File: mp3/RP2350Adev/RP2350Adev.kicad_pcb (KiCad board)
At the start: 2 copper layers, 30.9 x 51.8 mm, 44 parts, among them J1 USB4105-GF-A, J2 LEFT, J4 RIGHT, U1 W25Q32JV, U2 RP2350A, U3 MCP1702T-3302E_CB, X1 IQXO-791

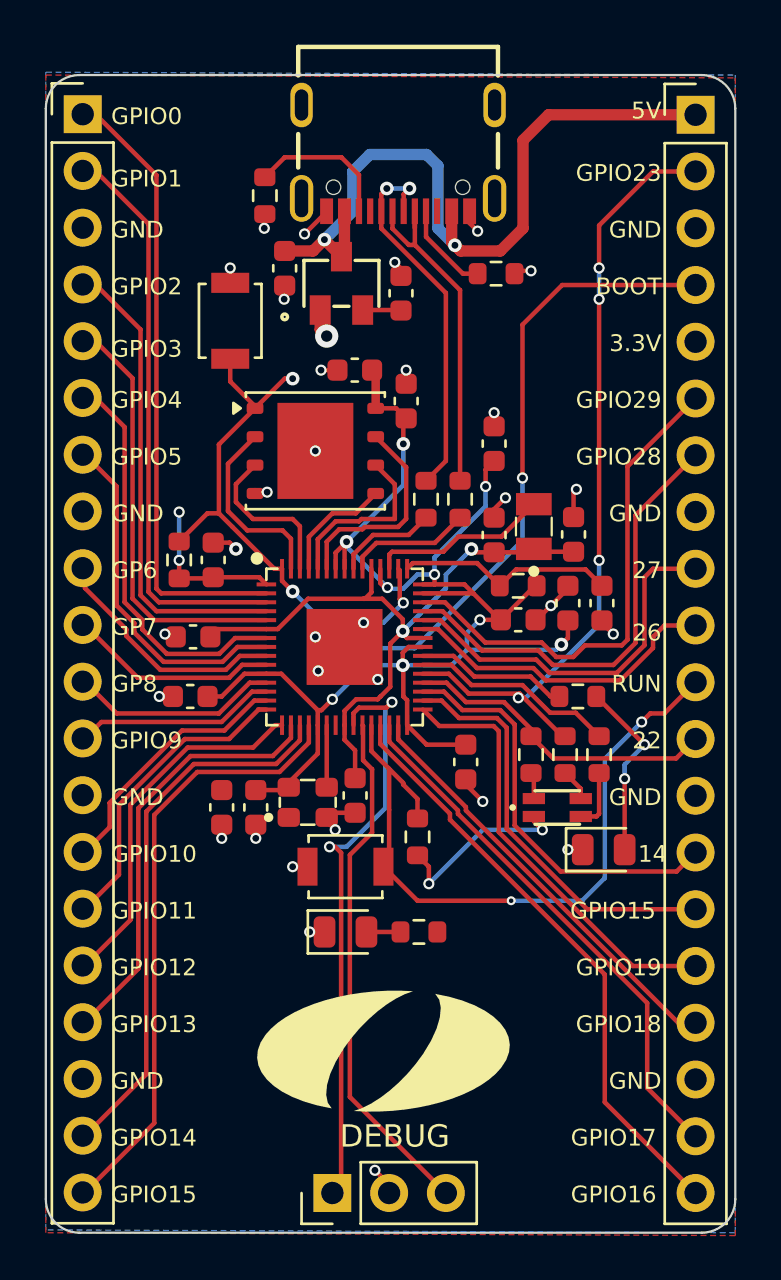
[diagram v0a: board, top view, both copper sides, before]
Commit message: Update silkscreen thickness/width for DRC
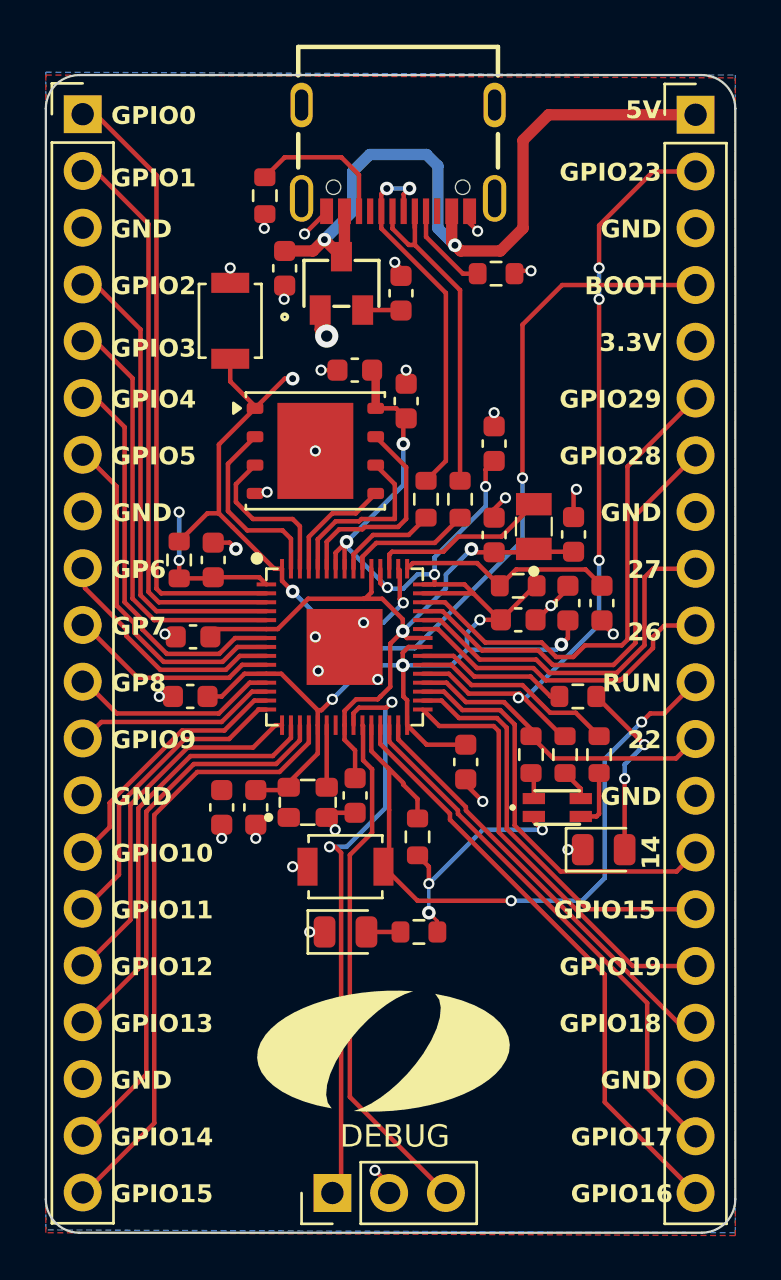
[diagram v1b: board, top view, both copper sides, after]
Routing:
- net +3V3: track 86.2 -> 88.5 mm, vias 13 -> 14
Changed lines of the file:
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@@
 		(effects
 			(font
-				(size 0.75 0.75)
-				(thickness 0.12)
+				(size 0.8 0.8)
+				(thickness 0.15)
+				(bold yes)
 			)
 			(justify right bottom)
@@
 		(effects
 			(font
-				(size 0.75 0.75)
-				(thickness 0.12)
+				(size 0.8 0.8)
+				(thickness 0.15)
+				(bold yes)
 			)
 			(justify left bottom)
@@
 		(effects
 			(font
-				(size 0.75 0.75)
-				(thickness 0.12)
+				(size 0.8 0.8)
+				(thickness 0.15)
+				(bold yes)
 			)
 			(justify right bottom)
@@
 		(effects
 			(font
-				(size 0.75 0.75)
-				(thickness 0.12)
+				(size 0.8 0.8)
+				(thickness 0.15)
+				(bold yes)
 			)
 			(justify left bottom)
@@
 		(effects
 			(font
-				(size 0.75 0.75)
-				(thickness 0.12)
+				(size 0.8 0.8)
+				(thickness 0.15)
+				(bold yes)
 			)
 			(justify right bottom)
@@
 		(effects
 			(font
-				(size 0.75 0.75)
-				(thickness 0.12)
+				(size 0.8 0.8)
+				(thickness 0.15)
+				(bold yes)
 			)
 			(justify right bottom)
@@
 		(effects
 			(font
-				(size 0.75 0.75)
-				(thickness 0.12)
+				(size 0.8 0.8)
+				(thickness 0.15)
+				(bold yes)
 			)
 			(justify left bottom)
@@
 		(effects
 			(font
-				(size 0.75 0.75)
-				(thickness 0.12)
+				(size 0.8 0.8)
+				(thickness 0.15)
+				(bold yes)
 			)
 			(justify right bottom)
@@
 		(effects
 			(font
-				(size 0.75 0.75)
-				(thickness 0.12)
+				(size 0.8 0.8)
+				(thickness 0.15)
+				(bold yes)
 			)
 			(justify left bottom)
@@
 		(effects
 			(font
-				(size 0.75 0.75)
-				(thickness 0.12)
+				(size 0.8 0.8)
+				(thickness 0.15)
+				(bold yes)
 			)
 			(justify right bottom)
@@
 		(effects
 			(font
-				(size 0.75 0.75)
-				(thickness 0.12)
+				(size 0.8 0.8)
+				(thickness 0.15)
+				(bold yes)
 			)
 			(justify left bottom)
@@
 		(effects
 			(font
-				(size 0.75 0.75)
-				(thickness 0.12)
+				(size 0.8 0.8)
+				(thickness 0.15)
+				(bold yes)
 			)
 			(justify left bottom)
@@
 		(effects
 			(font
-				(size 0.75 0.75)
-				(thickness 0.12)
+				(size 0.8 0.8)
+				(thickness 0.15)
+				(bold yes)
 			)
 			(justify right bottom)
@@
 		(effects
 			(font
-				(size 0.75 0.75)
-				(thickness 0.12)
+				(size 0.8 0.8)
+				(thickness 0.15)
+				(bold yes)
 			)
 			(justify right bottom)
@@
 		(effects
 			(font
-				(size 0.75 0.75)
-				(thickness 0.12)
+				(size 0.8 0.8)
+				(thickness 0.15)
+				(bold yes)
 			)
 			(justify left bottom)
@@
 		(effects
 			(font
-				(size 0.75 0.75)
-				(thickness 0.12)
+				(size 0.8 0.8)
+				(thickness 0.15)
+				(bold yes)
 			)
 			(justify left bottom)
@@
 		(effects
 			(font
-				(size 0.75 0.75)
-				(thickness 0.12)
+				(size 0.8 0.8)
+				(thickness 0.15)
+				(bold yes)
 			)
 			(justify left bottom)
@@
 		(effects
 			(font
-				(size 0.75 0.75)
-				(thickness 0.12)
+				(size 0.8 0.8)
+				(thickness 0.15)
+				(bold yes)
 			)
 			(justify left bottom)
@@
 		(effects
 			(font
-				(size 0.75 0.75)
-				(thickness 0.12)
+				(size 0.8 0.8)
+				(thickness 0.15)
+				(bold yes)
 			)
 			(justify left bottom)
@@
 		(effects
 			(font
-				(size 0.75 0.75)
-				(thickness 0.12)
+				(size 0.8 0.8)
+				(thickness 0.15)
+				(bold yes)
 			)
 			(justify left bottom)
@@
 		(effects
 			(font
-				(size 0.75 0.75)
-				(thickness 0.12)
+				(size 0.8 0.8)
+				(thickness 0.15)
+				(bold yes)
 			)
 			(justify right bottom)
@@
 		(effects
 			(font
-				(size 0.75 0.75)
-				(thickness 0.12)
+				(size 0.8 0.8)
+				(thickness 0.15)
+				(bold yes)
 			)
 			(justify right bottom)
@@
 		(effects
 			(font
-				(size 0.75 0.75)
-				(thickness 0.12)
+				(size 0.8 0.8)
+				(thickness 0.15)
+				(bold yes)
 			)
 			(justify right bottom)
@@
 		(effects
 			(font
-				(size 0.75 0.75)
-				(thickness 0.12)
+				(size 0.8 0.8)
+				(thickness 0.15)
+				(bold yes)
 			)
 			(justify left bottom)
@@
 		(effects
 			(font
-				(size 0.75 0.75)
-				(thickness 0.12)
+				(size 0.8 0.8)
+				(thickness 0.15)
+				(bold yes)
 			)
 			(justify left bottom)
@@
 		(effects
 			(font
-				(size 0.75 0.75)
-				(thickness 0.12)
+				(size 0.8 0.8)
+				(thickness 0.15)
+				(bold yes)
 			)
 			(justify left bottom)
@@
 		(effects
 			(font
-				(size 0.75 0.75)
-				(thickness 0.12)
+				(size 0.8 0.8)
+				(thickness 0.15)
+				(bold yes)
 			)
 			(justify right bottom)
@@
 	)
 	(gr_text "14"
-		(at 55.118 58.166 0)
+		(at 54.864 56.896 90)
 		(layer "F.SilkS")
 		(effects
 			(font
-				(size 0.75 0.75)
-				(thickness 0.12)
+				(size 0.8 0.8)
+				(thickness 0.15)
+				(bold yes)
 			)
 			(justify right bottom)
@@
 		(effects
 			(font
-				(size 0.75 0.75)
-				(thickness 0.12)
+				(size 0.8 0.8)
+				(thickness 0.15)
+				(bold yes)
 			)
 			(justify right bottom)
@@
 		(effects
 			(font
-				(size 0.75 0.75)
-				(thickness 0.12)
+				(size 0.8 0.8)
+				(thickness 0.15)
+				(bold yes)
 			)
 			(justify left bottom)
@@
 		(effects
 			(font
-				(size 0.75 0.75)
-				(thickness 0.12)
+				(size 0.8 0.8)
+				(thickness 0.15)
+				(bold yes)
 			)
 			(justify left bottom)
@@
 		(effects
 			(font
-				(size 0.75 0.75)
-				(thickness 0.12)
+				(size 0.8 0.8)
+				(thickness 0.15)
+				(bold yes)
 			)
 			(justify right bottom)
@@
 		(effects
 			(font
-				(size 0.75 0.75)
-				(thickness 0.12)
+				(size 0.8 0.8)
+				(thickness 0.15)
+				(bold yes)
 			)
 			(justify right bottom)
@@
 		(effects
 			(font
-				(size 0.75 0.75)
-				(thickness 0.12)
+				(size 0.8 0.8)
+				(thickness 0.15)
+				(bold yes)
 			)
 			(justify left bottom)
@@
 		(effects
 			(font
-				(size 0.75 0.75)
-				(thickness 0.12)
+				(size 0.8 0.8)
+				(thickness 0.15)
+				(bold yes)
 			)
 			(justify left bottom)
@@
 		(effects
 			(font
-				(size 0.75 0.75)
-				(thickness 0.12)
+				(size 0.8 0.8)
+				(thickness 0.15)
+				(bold yes)
 			)
 			(justify left bottom)
@@
 		(effects
 			(font
-				(size 0.75 0.75)
-				(thickness 0.12)
+				(size 0.8 0.8)
+				(thickness 0.15)
+				(bold yes)
 			)
 			(justify left bottom)
@@
 		(effects
 			(font
-				(size 0.75 0.75)
-				(thickness 0.12)
+				(size 0.8 0.8)
+				(thickness 0.15)
+				(bold yes)
 			)
 			(justify right bottom)
@@
 		(effects
 			(font
-				(size 0.75 0.75)
-				(thickness 0.12)
+				(size 0.8 0.8)
+				(thickness 0.15)
+				(bold yes)
 			)
 			(justify right bottom)
@@
 		(effects
 			(font
-				(size 0.75 0.75)
-				(thickness 0.12)
+				(size 0.8 0.8)
+				(thickness 0.15)
+				(bold yes)
 			)
 			(justify left bottom)
@@
 	)
 	(segment
+		(start 44.83 61.214)
+		(end 44.83 60.7304)
+		(width 0.1524)
+		(layer "F.Cu")
+		(net 1)
+	)
+	(segment
 		(start 42.07 37.778)
 		(end 42.07 36.228)
@@
 	)
 	(segment
+		(start 44.83 60.7304)
+		(end 44.45 60.3504)
+		(width 0.1524)
+		(layer "F.Cu")
+		(net 1)
+	)
+	(segment
 		(start 50.380822 48.348822)
 		(end 50.673 48.056644)
@@
 	)
 	(via
+		(at 44.45 60.3504)
+		(size 0.6096)
+		(drill 0.3048)
+		(layers "F.Cu" "B.Cu")
+		(net 1)
+	)
+	(via
 		(at 44.704 45.212)
 		(size 0.5)
@@
 	)
 	(segment
+		(start 44.45 60.3504)
+		(end 44.45 59.055)
+		(width 0.1524)
+		(layer "B.Cu")
+		(net 1)
+	)
+	(segment
 		(start 42.596197 45.797902)
 		(end 42.596197 45.668803)
@@
 	(via
 		(at 48.133 59.817)
-		(size 0.4)
-		(drill 0.2)
+		(size 0.5)
+		(drill 0.3)
 		(layers "F.Cu" "B.Cu")
 		(net 44)

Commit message: Update silkscreen overlap
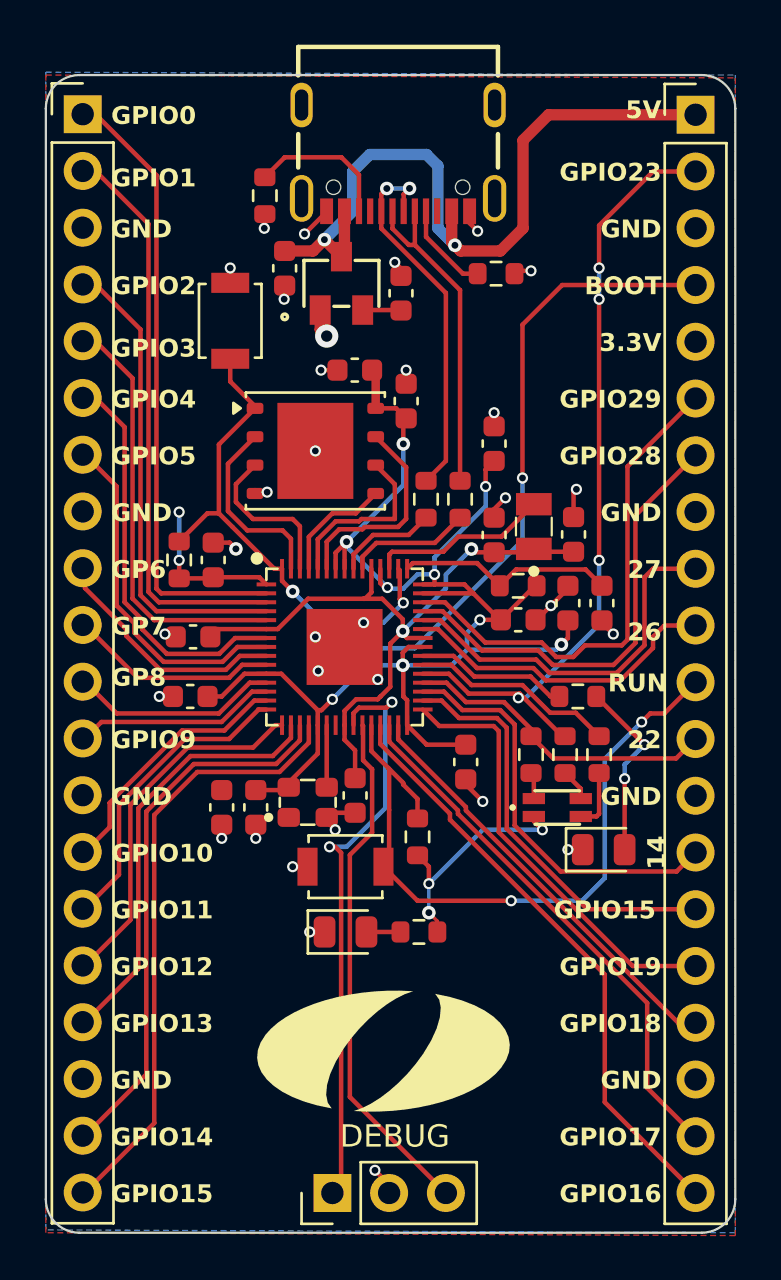
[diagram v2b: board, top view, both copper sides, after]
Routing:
- net /BOOT: track 49.3 -> 47.1 mm, vias 3 -> 2
- net Net-(J1-D--PadA7): track 15.7 -> 15.0 mm
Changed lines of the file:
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@@
 	)
 	(gr_text "RUN"
-		(at 54.864 50.546 0)
+		(at 55.118 50.546 0)
 		(layer "F.SilkS")
 		(effects
@@
 	)
 	(gr_text "GPIO17"
-		(at 50.8 70.866 0)
+		(at 50.292 70.866 0)
 		(layer "F.SilkS")
 		(effects
@@
 	)
 	(gr_text "GP8"
-		(at 30.226 50.546 0)
+		(at 30.226 50.292 0)
 		(layer "F.SilkS")
 		(effects
@@
 	)
 	(gr_text "14"
-		(at 54.864 56.896 90)
+		(at 55.118 56.896 90)
 		(layer "F.SilkS")
 		(effects
@@
 	)
 	(gr_text "GPIO16"
-		(at 50.8 73.406 0)
+		(at 50.292 73.406 0)
 		(layer "F.SilkS")
 		(effects
@@
 	)
 	(segment
-		(start 44.352 52.832)
-		(end 43.478 51.958)
-		(width 0.2032)
-		(layer "F.Cu")
-		(net 1)
-	)
-	(segment
 		(start 39.478 51.289)
 		(end 39.478 51.958)
@@
 	)
 	(segment
-		(start 45.974 52.832)
-		(end 44.352 52.832)
-		(width 0.2032)
-		(layer "F.Cu")
-		(net 1)
-	)
-	(segment
 		(start 38.051 54.864)
 		(end 38.178 54.737)
@@
 	)
 	(segment
+		(start 44.352 52.832)
+		(end 43.478 51.958)
+		(width 0.2032)
+		(layer "F.Cu")
+		(net 1)
+	)
+	(segment
 		(start 44.83 60.7304)
 		(end 44.45 60.3504)
@@
 	)
 	(segment
+		(start 45.974 52.832)
+		(end 44.352 52.832)
+		(width 0.2032)
+		(layer "F.Cu")
+		(net 1)
+	)
+	(segment
 		(start 49.149 56.261)
 		(end 49.53 56.642)
@@
 	)
 	(segment
-		(start 43.823 29.702)
-		(end 43.823 28.956)
-		(width 0.2032)
-		(layer "F.Cu")
-		(net 14)
-	)
-	(segment
 		(start 45.847 41.021)
 		(end 45.847 32.488)
@@
 	)
 	(segment
-		(start 36.67 37.778)
-		(end 37.999 36.449)
-		(width 0.2032)
-		(layer "F.Cu")
-		(net 45)
-	)
-	(segment
 		(start 50.419 32.258)
 		(end 48.641 34.036)
@@
 	)
 	(segment
-		(start 37.999 36.449)
-		(end 38.354 36.449)
-		(width 0.2032)
-		(layer "F.Cu")
-		(net 45)
-	)
-	(segment
 		(start 36.67 37.686)
 		(end 35.56 36.576)
@@
 		(layers "F.Cu" "B.Cu")
 		(net 45)
-	)
-	(via
-		(at 38.354 36.449)
-		(size 0.6096)
-		(drill 0.3048)
-		(layers "F.Cu" "B.Cu")
-		(net 45)

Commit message: Update minimum via size to 24 mils
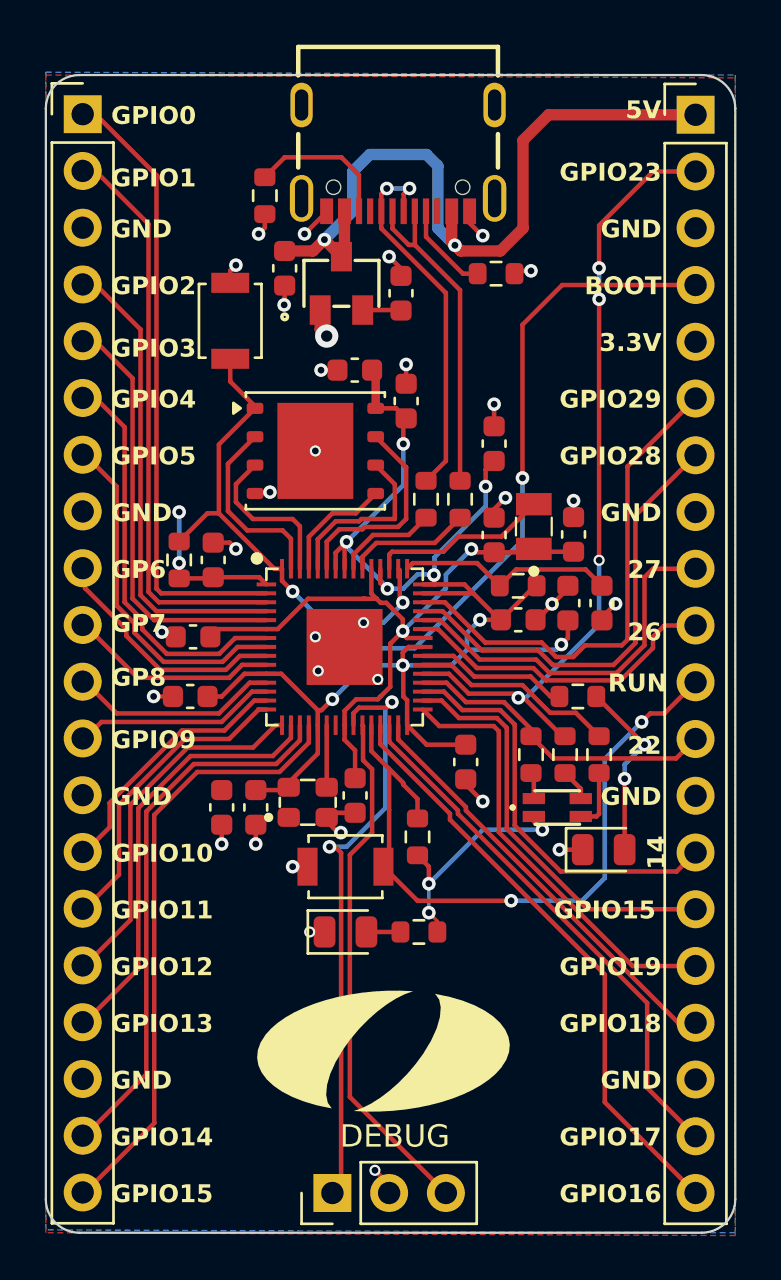
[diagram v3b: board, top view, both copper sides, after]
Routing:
- net GND: track 37.4 -> 40.9 mm

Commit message: Update missed undersized vias to 24 mils
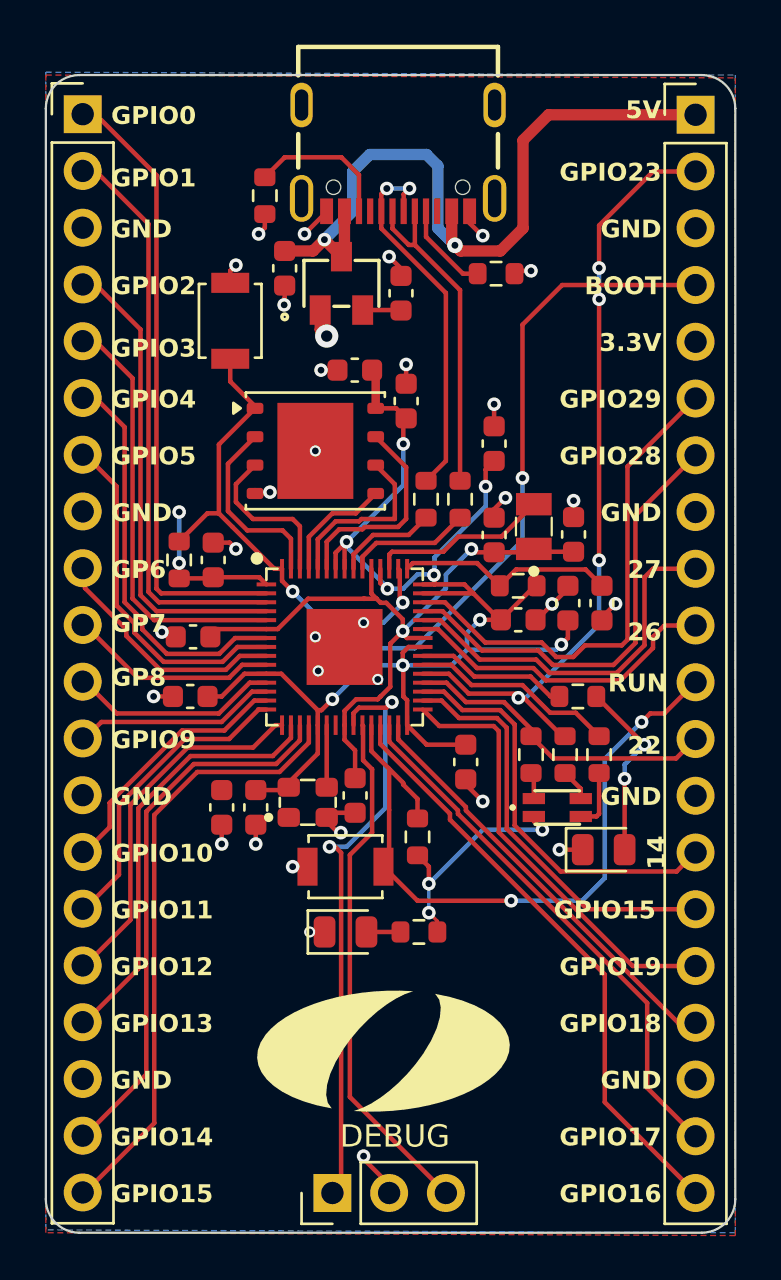
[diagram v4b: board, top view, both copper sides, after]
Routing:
- net GND: track 40.9 -> 41.7 mm
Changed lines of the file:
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@@
-	)
-	(segment
-		(start 42.672 72.517)
-		(end 42.037 71.882)
-		(width 0.2032)
-		(layer "F.Cu")
-		(net 2)
 	)
 	(segment
@@
 	)
 	(segment
+		(start 42.672 72.517)
+		(end 42.672 72.898)
+		(width 0.2032)
+		(layer "F.Cu")
+		(net 2)
+	)
+	(segment
 		(start 43.146799 45.026799)
 		(end 43.078 44.958)
@@
 	)
 	(segment
+		(start 41.529 71.247)
+		(end 41.529 71.374)
+		(width 0.2032)
+		(layer "F.Cu")
+		(net 2)
+	)
+	(segment
 		(start 32.500683 47.791399)
 		(end 32.551399 47.791399)
@@
 	)
 	(segment
-		(start 42.672 72.898)
-		(end 42.672 72.517)
-		(width 0.2032)
-		(layer "F.Cu")
-		(net 2)
-	)
-	(segment
 		(start 37.338 41.529)
 		(end 37.211 41.529)
@@
 	)
 	(segment
+		(start 41.529 71.374)
+		(end 42.672 72.517)
+		(width 0.2032)
+		(layer "F.Cu")
+		(net 2)
+	)
+	(segment
 		(start 37.152 41.588)
 		(end 36.67 41.588)
@@
 	)
 	(via
-		(at 42.037 71.882)
-		(size 0.5)
+		(at 41.529 71.247)
+		(size 0.6096)
 		(drill 0.3)
 		(layers "F.Cu" "B.Cu")
@@
 	(via
 		(at 45.617 30.48)
-		(size 0.6096)
+		(size 0.7)
 		(drill 0.3048)
 		(layers "F.Cu" "B.Cu")
@@
 	(via
 		(at 52.07 44.577)
-		(size 0.5)
-		(drill 0.3)
-		(layers "F.Cu" "B.Cu")
+		(size 0.6096)
+		(drill 0.3)
+		(layers "F.Cu" "B.Cu")

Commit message: Update ground pad vias to 24 mils
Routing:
- net GND: track 41.7 -> 42.2 mm, vias 33 -> 32
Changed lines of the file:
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@@
+	)
+	(segment
+		(start 50.927 41.656)
+		(end 50.927 42.646)
+		(width 0.2032)
+		(layer "F.Cu")
+		(net 2)
 	)
 	(segment
@@
 		(start 40.569 48.458)
 		(end 39.497 49.53)
+		(width 0.2032)
+		(layer "F.Cu")
+		(net 2)
+	)
+	(segment
+		(start 39.781 61.214)
+		(end 38.862 61.214)
 		(width 0.2032)
 		(layer "F.Cu")
@@
 	)
 	(segment
-		(start 39.781 61.214)
-		(end 39.116 61.214)
-		(width 0.2032)
-		(layer "F.Cu")
-		(net 2)
-	)
-	(segment
 		(start 35.179 56.414)
 		(end 35.179 57.277)
@@
 	)
 	(segment
-		(start 50.927 41.91)
-		(end 50.927 42.646)
-		(width 0.2032)
-		(layer "F.Cu")
-		(net 2)
-	)
-	(segment
 		(start 37.973 33.147)
 		(end 37.973 32.893)
@@
 	(via
 		(at 39.37 48.006)
-		(size 0.5)
+		(size 0.6096)
 		(drill 0.3)
 		(layers "F.Cu" "B.Cu")
@@
 	(via
 		(at 39.37 39.683)
-		(size 0.5)
-		(drill 0.3)
-		(layers "F.Cu" "B.Cu")
-		(net 2)
-	)
-	(via
-		(at 42.164 49.911)
-		(size 0.5)
+		(size 0.6096)
 		(drill 0.3)
 		(layers "F.Cu" "B.Cu")
@@
 	)
 	(via
-		(at 39.116 61.214)
-		(size 0.5)
+		(at 38.862 61.214)
+		(size 0.6096)
 		(drill 0.3)
 		(layers "F.Cu" "B.Cu")
@@
 	)
 	(via
-		(at 50.927 41.91)
+		(at 50.927 41.656)
 		(size 0.6096)
 		(drill 0.3)
@@
 	(via
 		(at 41.529 47.371)
-		(size 0.5)
+		(size 0.6096)
 		(drill 0.3)
 		(layers "F.Cu" "B.Cu")
@@
 	(via
 		(at 39.497 49.53)
-		(size 0.5)
-		(drill 0.3)
-		(layers "F.Cu" "B.Cu")
+		(size 0.6096)
+		(drill 0.3)
+		(layers "F.Cu" "B.Cu")
